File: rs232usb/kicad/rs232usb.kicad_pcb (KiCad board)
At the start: 2 copper layers, 28.1 x 13.5 mm, 13 parts, among them J1 USB_C_Receptacle_USB2.0_14P, J2 DE9_Socket, U1 CH340N, U2 MAX232

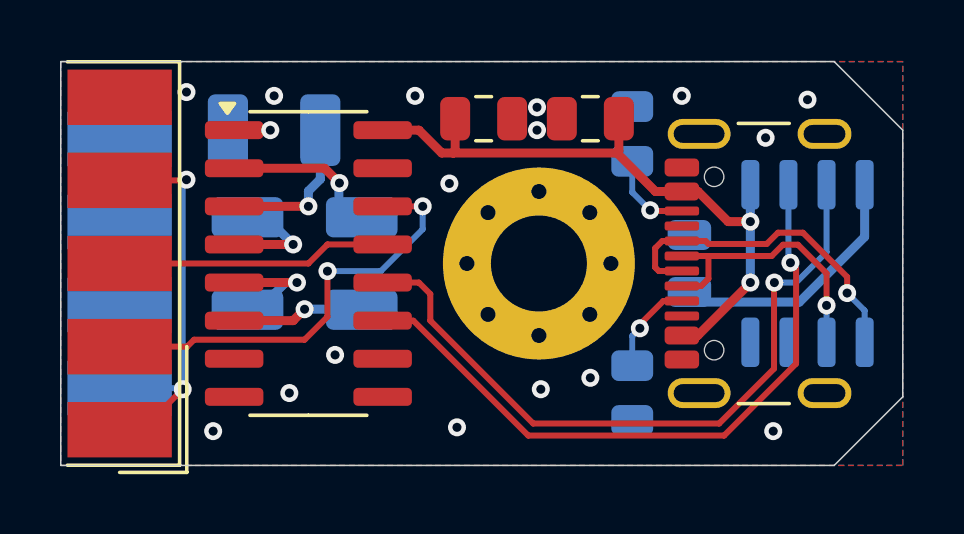
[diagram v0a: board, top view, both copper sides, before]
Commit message: Fix rs232usb wrong MAX232 setup
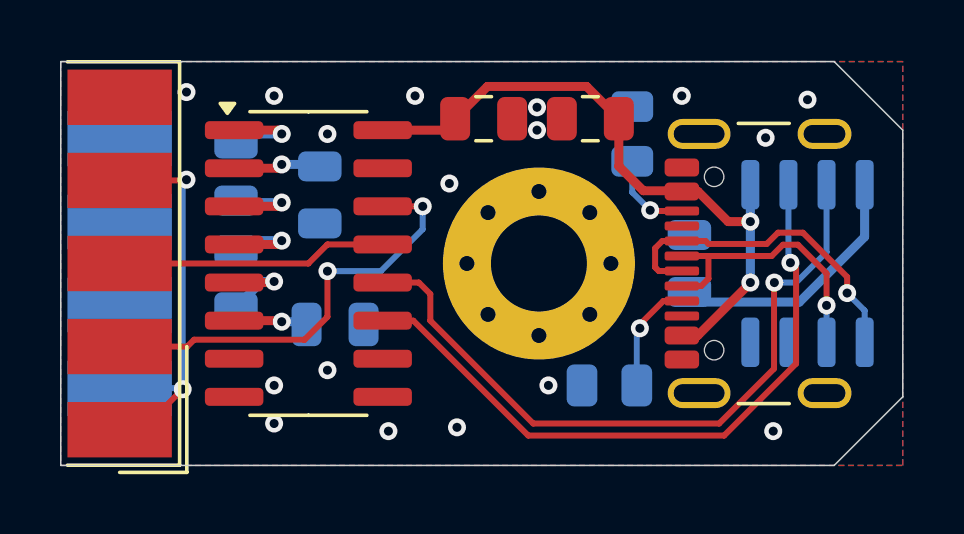
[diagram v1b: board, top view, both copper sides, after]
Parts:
- removed C2, C3, C4: 22u, Capacitor_Tantalum_SMD:CP_EIA-3528-12_Kemet-T
- added C10: 1u, Capacitor_SMD:C_0805_2012Metric, B.Cu at (116.1, 73.2)
- added C7: 1u, Capacitor_SMD:C_0805_2012Metric, B.Cu at (112.8, 68.1)
- added C8: 1u, Capacitor_SMD:C_0805_2012Metric, B.Cu at (112.8, 71.6)
- added C9: 1u, Capacitor_SMD:C_0805_2012Metric, B.Cu at (115.6, 68.8)
- moved R1 0.80 mm to (125.2, 75.2), turned to 180 degrees
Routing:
- net Net-(U2-VS+): track 5.34 -> 2.94 mm
- net Net-(U2-C1-): track 5.18 -> 3.19 mm
- net Net-(U2-VS-): track 4.42 -> 2.47 mm
- net Net-(U2-C2-): track 4.12 -> 2.97 mm
- net Net-(U2-C1+): track 2.62 -> 3.30 mm
- net Net-(J1-CC1): track 3.20 -> 3.80 mm
- net Net-(U2-C2+): track 3.87 -> 3.30 mm
- net GND: vias 16 -> 17
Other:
- board text added: "Rev B"
